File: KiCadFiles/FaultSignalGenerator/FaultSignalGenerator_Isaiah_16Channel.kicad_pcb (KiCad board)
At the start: 4 copper layers, 280 parts, among them J1 Conn_02x20_Odd_Even, J2 Conn_02x16_Odd_Even, J3 DB25_Receptacle, U1 MCP4431-503E/ST, U10 TL074CDR, U11 TL074CDR, U12 TL074CDR, U13 TL074CDR, U14 PCM1681PWP, U15 PCM1681PWP, U16 TL780-05CKTTR, U2 MCP4431-503E/ST, U3 MCP4431-503E/ST, U4 MCP4431-503E/ST, U5 TL074CDR, U6 TL074CDR, U7 TL074CDR, U8 TL074CDR, U9 TL074CDR

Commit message: changes to make board smaller
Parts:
- moved C79 239.6 mm to (57.4, 132.2), turned to 90 degrees
- moved C80 230.9 mm to (63.8, 134.7), turned to 180 degrees
- moved J1 220.5 mm to (58.9, 80.8)
- moved C84 219.9 mm to (70.1, 134.7), turned to 0 degrees
- moved U16 213.6 mm to (66.6, 121.1), turned to 90 degrees
- moved D1 205.3 mm to (76.7, 131.4), turned to 90 degrees
- moved C83 198.7 mm to (81.8, 133.2), turned to -90 degrees
- moved L1 197.4 mm to (76.8, 123.6), turned to -90 degrees
- moved R94 196.9 mm to (71.2, 59.9), turned to 0 degrees
- moved R97 195.7 mm to (71.2, 62.2), turned to 0 degrees
- moved C30 195.1 mm to (71.1, 108.4), turned to 180 degrees
- moved R99 194.6 mm to (71.2, 64.5), turned to 0 degrees
- moved R142 194.0 mm to (85.8, 134.8), turned to 180 degrees
- moved R93 193.9 mm to (71.2, 106.1), turned to 0 degrees
- moved R95 193.7 mm to (71.2, 66.8), turned to 0 degrees
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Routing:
- net 0: track 924.2 -> 490.1 mm, vias 62 -> 35
- net +12V: track 363.1 -> 181.2 mm, vias 7 -> 5
- net LED1: track 143.5 -> 0.00 mm
- net LED9: track 130.4 -> 0.00 mm
- net LED2: track 126.9 -> 0.00 mm
- net LED10: track 121.5 -> 0.00 mm
- net LED3: track 119.5 -> 0.00 mm
- net LED4: track 118.3 -> 0.00 mm
- net LED11: track 112.3 -> 0.00 mm
- net LED5: track 106.5 -> 0.00 mm
- net LED12: track 100.2 -> 0.00 mm
- net LED6: track 99.4 -> 0.00 mm
- net LED13: track 98.8 -> 0.00 mm
- net LED8: track 95.4 -> 0.00 mm
- net LED15: track 93.4 -> 0.00 mm
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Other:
- board text removed: "DAC Connection"
- board text removed: "Pi Connection"
- board text removed: "Power Block"

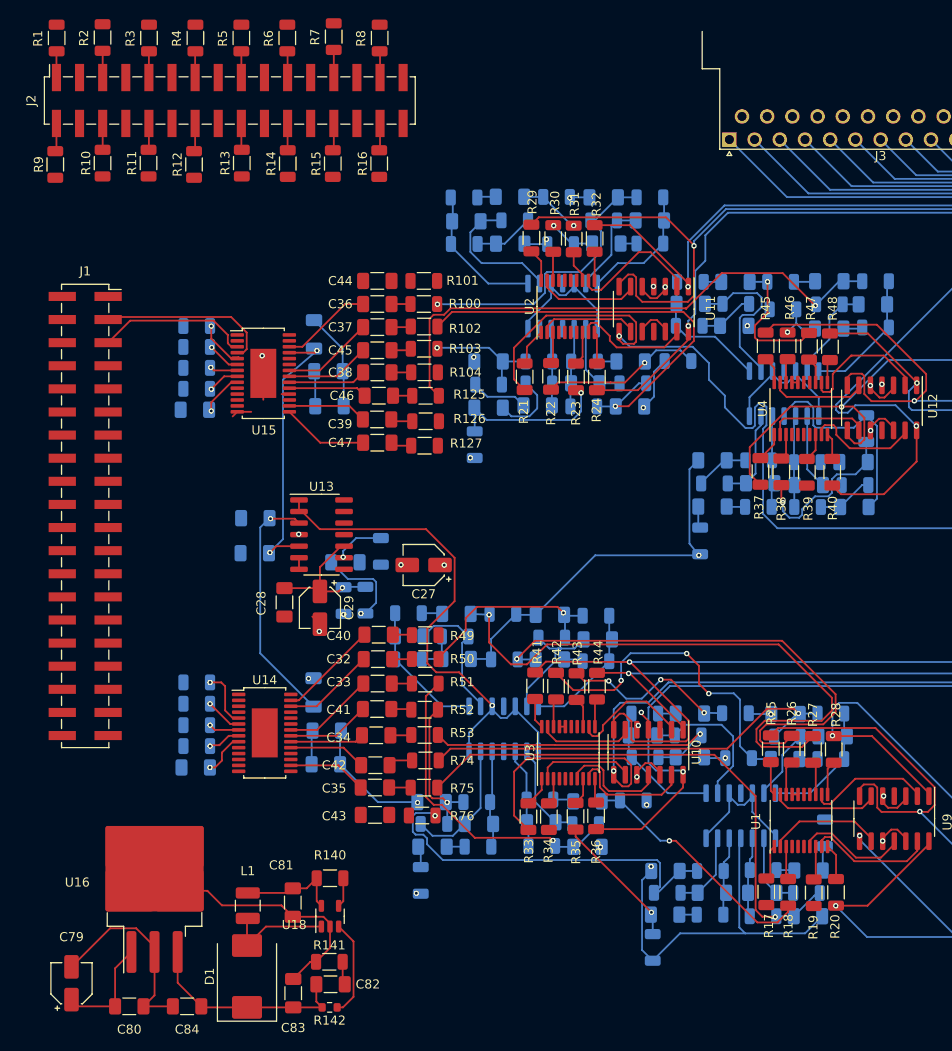
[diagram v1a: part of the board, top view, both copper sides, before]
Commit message: Power connections + ground plane + data connections
Everything is hooked up except for the final SCL and SDA pins. I want to run them along the ground plane, but unsure if that'll cause data corruption due to EMI. Also, power connections might need to be revamped since I didn't think about series connections being a problem between components. However, this does become an issue as draw begins to increase down a single trace.
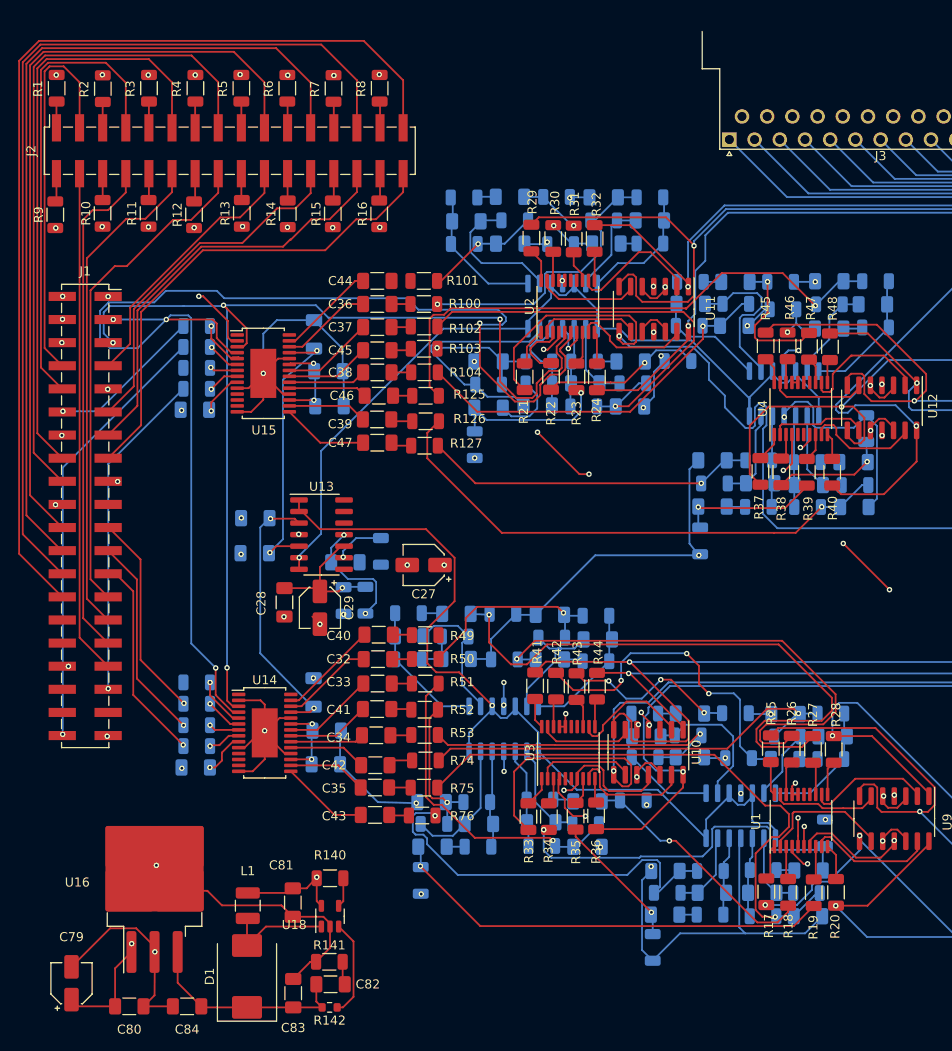
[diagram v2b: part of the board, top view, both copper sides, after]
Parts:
- moved R7 5.69 mm to (86.2, 33.8)
- moved R2 5.62 mm to (60.9, 33.8)
- moved R14 5.52 mm to (81.2, 47.6)
- moved R15 5.52 mm to (86.1, 47.6)
- moved R16 5.52 mm to (91.2, 47.6)
- moved J2 5.52 mm to (74.8, 40.7)
- moved R1 5.52 mm to (55.8, 33.8)
- moved R10 5.52 mm to (60.8, 47.5)
- moved R11 5.52 mm to (65.9, 47.5)
- moved R12 5.52 mm to (70.9, 47.7)
- moved R13 5.52 mm to (76.1, 47.5)
- moved R3 5.52 mm to (65.9, 33.8)
- moved R4 5.52 mm to (71.0, 33.8)
- moved R5 5.52 mm to (76.1, 33.8)
- moved R6 5.52 mm to (81.1, 33.8)
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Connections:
- J1 pad 10: LED6 -> LED2
- J1 pad 11: LED1 -> LED14
- J1 pad 13: LED2 -> LED15
- J1 pad 15: LED3 -> LED16
- J1 pad 16: LED7 -> LED3
- J1 pad 18: LED12 -> LED4
- J1 pad 22: LED14 -> LED5
- J1 pad 24: LED15 -> LED6
- J1 pad 26: LED16 -> LED7
- J1 pad 27: LED8 -> LED12
- J1 pad 28: LED13 -> LED8
- J1 pad 29: LED9 -> LED11
- J1 pad 33: LED11 -> LED9
- J1 pad 7: LED4 -> LED13
- J1 pad 8: LED5 -> LED1
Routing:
- net +5V: track 20.1 -> 347.2 mm, vias 0 -> 22
- net SDA: track 19.1 -> 154.3 mm, vias 0 -> 5
- net +3.3V: track 9.57 -> 136.4 mm, vias 2 -> 5
- net LED8: track 0.00 -> 111.0 mm
- net SCL: track 16.9 -> 124.8 mm, vias 0 -> 5
- net LED7: track 0.00 -> 102.4 mm
- net +12V: track 181.2 -> 280.5 mm, vias 5 -> 8
- net LED6: track 0.00 -> 93.7 mm
- net LED5: track 0.00 -> 85.0 mm
- net LED4: track 0.00 -> 73.9 mm
- net LED3: track 0.00 -> 65.3 mm
- net +10: track 30.0 -> 92.9 mm, vias 0 -> 1
- net LED10: track 0.00 -> 55.7 mm
- net LED9: track 0.00 -> 55.4 mm
- net LED12: track 0.00 -> 55.1 mm
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- added copper zone on In1.Cu, net 0

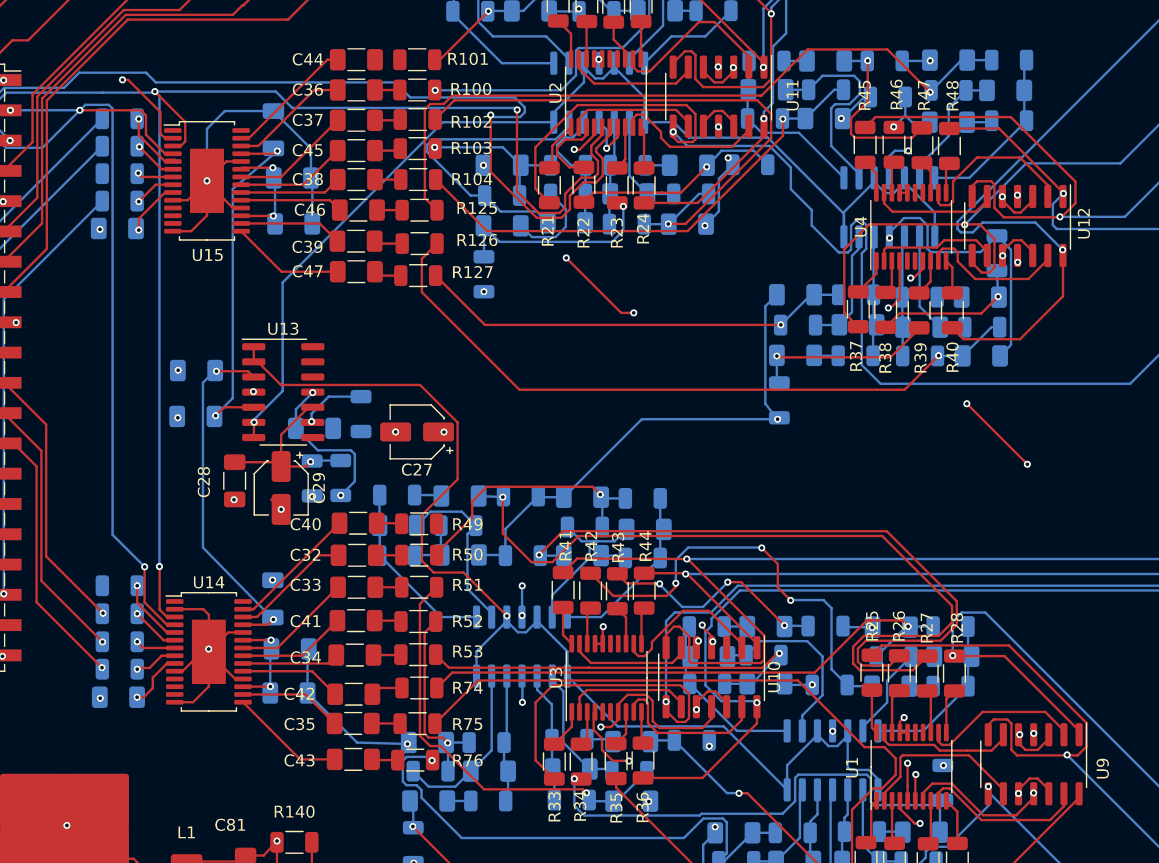
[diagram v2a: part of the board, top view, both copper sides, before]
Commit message: I2C connections
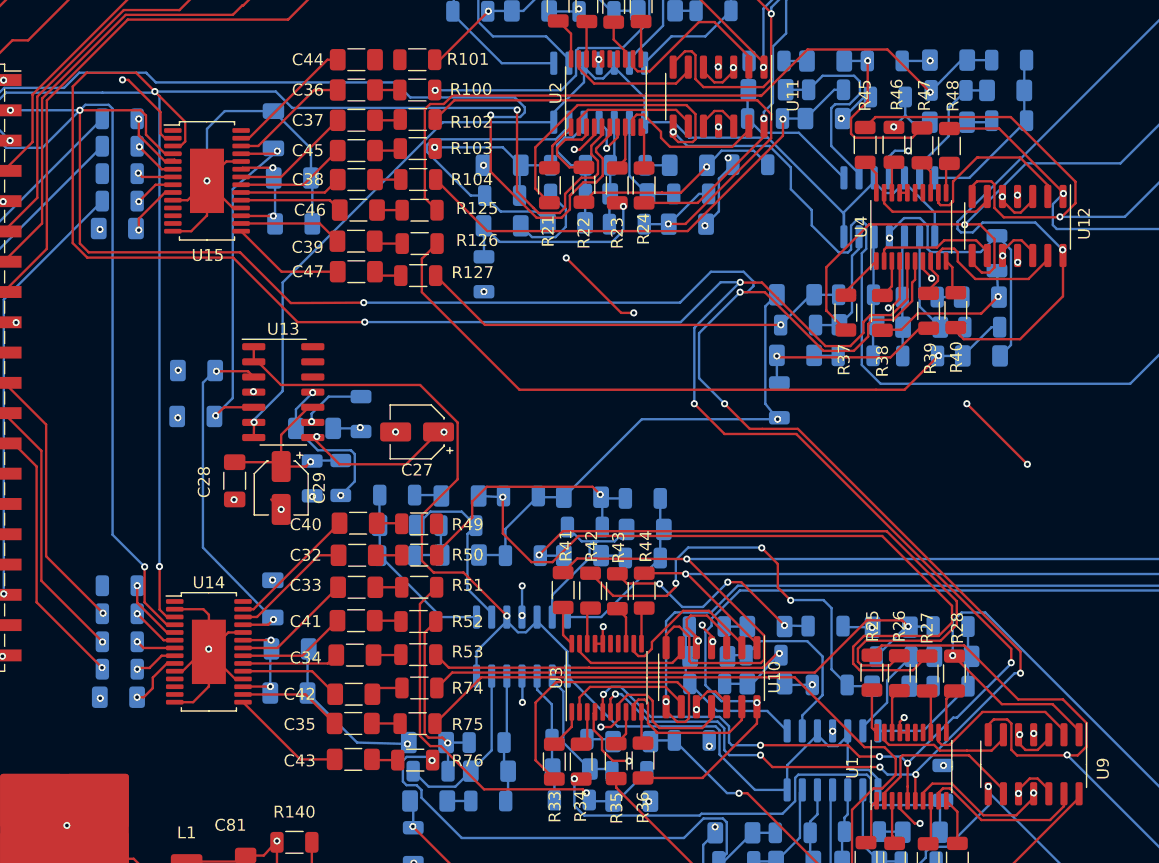
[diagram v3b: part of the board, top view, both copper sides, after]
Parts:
- moved R37 1.08 mm to (132.1, 76.2)
- moved R39 0.80 mm to (139.0, 76.0)
- moved R38 0.37 mm to (135.2, 76.2)
- moved R40 0.29 mm to (141.3, 76.0)
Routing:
- net SCL: track 124.8 -> 318.9 mm, vias 5 -> 12
- net SDA: track 154.3 -> 339.8 mm, vias 5 -> 12
- net +6V: track 186.4 -> 214.2 mm, vias 8 -> 10
- net +1: track 95.2 -> 96.4 mm
- net Channel15: track 54.3 -> 55.4 mm
- net Net-(U4-P3A): track 3.22 -> 4.19 mm
- net +5V: track 347.2 -> 348.1 mm
- net 0: track 491.6 -> 492.1 mm
